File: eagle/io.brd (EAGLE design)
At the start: 120.3 x 50.8 mm, 8 parts, among them IC1 MAX7219CNG, SW1 EC12E_SW, SW2 EC12E_SW, X1 22-23-2101, X2 22-23-2021

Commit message: Route IO board (badly)
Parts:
- moved R1 7.01 mm to (39.4, 21.6)
- moved SW1 2.54 mm to (25.4, 15.2)
- moved SW2 2.54 mm to (94.0, 15.2)
- moved X2 2.54 mm to (5.08, 17.8)
- moved IC1 2.54 mm to (59.7, 20.3)
- moved LED1 2.54 mm to (25.4, 40.6)
- moved LED2 2.54 mm to (94.0, 40.6)
- moved X1 0.32 mm to (59.7, 4.76)
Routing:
- net N$3: track 0.00 -> 140.8 mm, vias 0 -> 4
- net N$6: track 0.00 -> 140.5 mm, vias 0 -> 3
- net N$8: track 0.00 -> 118.3 mm, vias 0 -> 5
- net N$12: track 0.00 -> 101.4 mm
- net N$29: track 0.00 -> 97.3 mm, vias 0 -> 1
- net N$15: track 0.00 -> 90.5 mm, vias 0 -> 3
- net N$20: track 0.00 -> 89.6 mm
- net N$11: track 0.00 -> 89.0 mm, vias 0 -> 2
- net N$13: track 0.00 -> 88.3 mm
- net N$14: track 0.00 -> 87.8 mm
- net N$19: track 0.00 -> 86.7 mm, vias 0 -> 2
- net N$31: track 0.00 -> 72.5 mm, vias 0 -> 4
- net N$4: track 0.00 -> 69.3 mm, vias 0 -> 4
- net N$38: track 0.00 -> 67.2 mm
- net N$61: track 0.00 -> 64.1 mm, vias 0 -> 3
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- added copper zone on layer 16, net GND
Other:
- board size 120.3 x 50.8 mm -> 120.3 x 55.9 mm

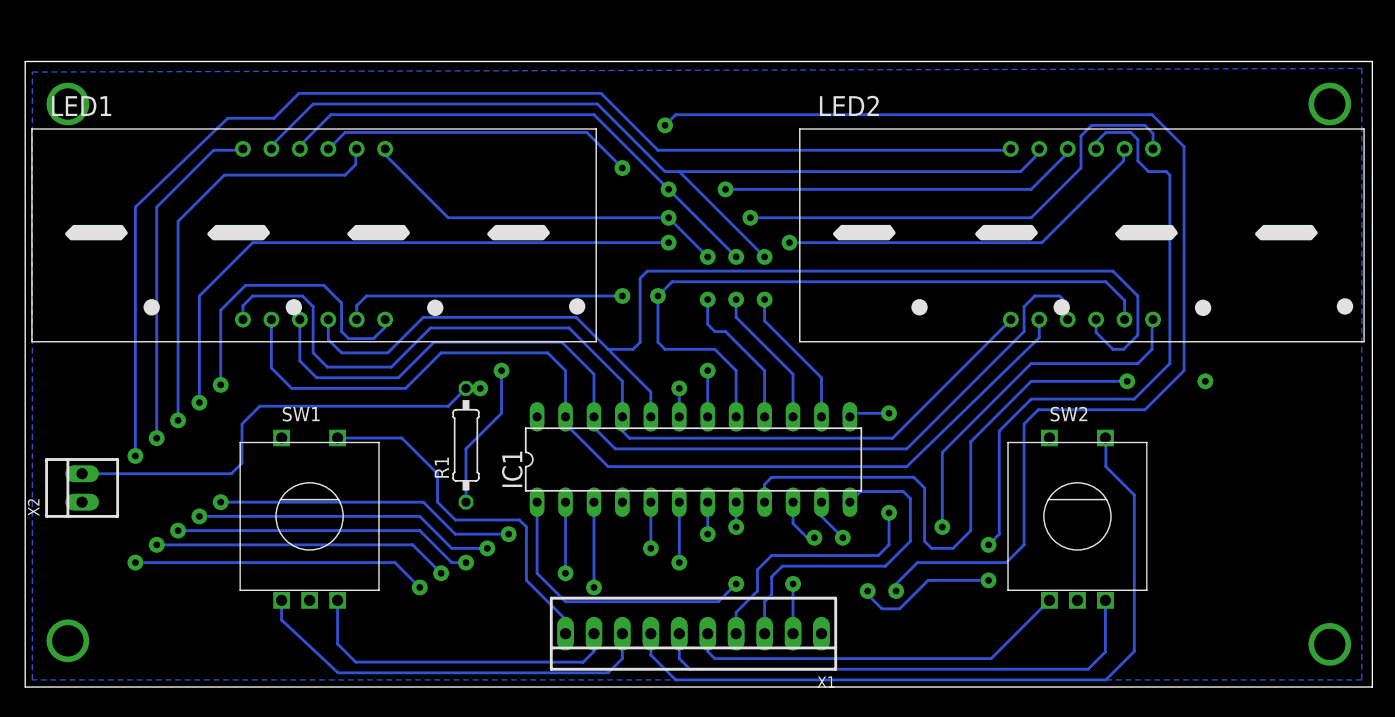
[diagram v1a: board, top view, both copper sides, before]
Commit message: Tighten up io board a bit, should be ready for etching
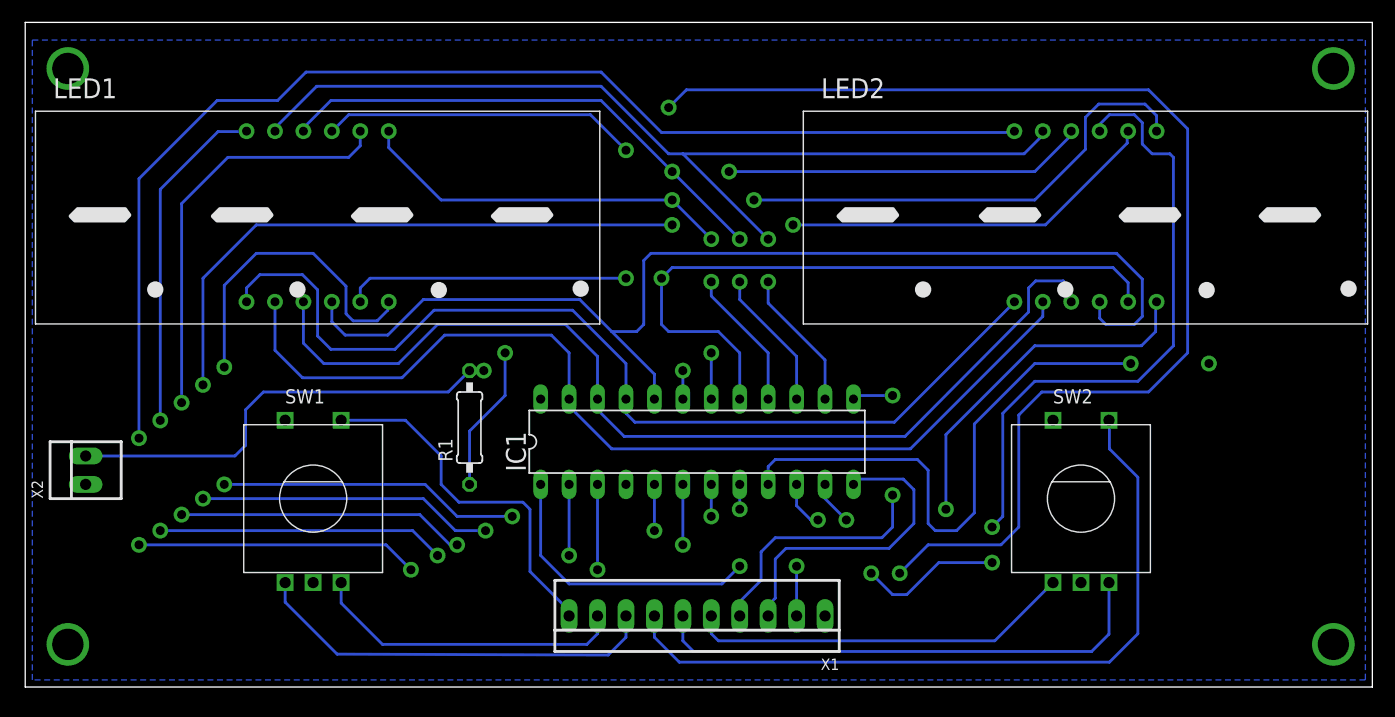
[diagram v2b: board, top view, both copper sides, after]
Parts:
- moved SW1 1.62 mm to (25.7, 16.8)
- moved X1 1.62 mm to (60.0, 6.35)
- moved SW2 1.62 mm to (94.3, 16.8)
- moved IC1 1.62 mm to (60.0, 21.9)
- moved LED1 1.62 mm to (25.7, 42.2)
- moved R1 1.62 mm to (39.7, 23.2)
- moved X2 1.62 mm to (5.40, 19.4)
- moved LED2 1.62 mm to (94.3, 42.2)
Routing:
- net N$61: track 64.1 -> 62.4 mm
- net N$55: track 56.8 -> 58.1 mm
- net N$40: track 29.4 -> 28.2 mm
- net N$4: track 69.3 -> 68.3 mm
- net N$1: track 28.9 -> 28.0 mm
- net N$17: track 17.8 -> 17.2 mm
- net VCC: track 43.6 -> 43.1 mm
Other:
- board size 120.3 x 55.9 mm -> 120.3 x 59.4 mm
